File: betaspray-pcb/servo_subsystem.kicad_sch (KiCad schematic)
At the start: 8 parts, among them J11 Conn_01x03_Pin, J12 Conn_01x03_Pin, J13 Conn_01x03_Pin, J14 Conn_01x03_Pin, J15 Conn_01x03_Pin, J16 Conn_01x03_Pin, J17 Conn_01x03_Pin, J18 Conn_01x03_Pin

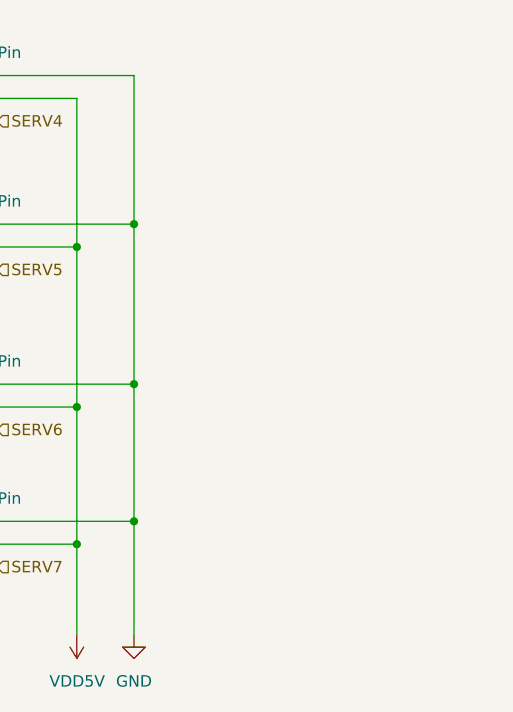
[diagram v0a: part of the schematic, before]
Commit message: Added lasers to schematic and footprint
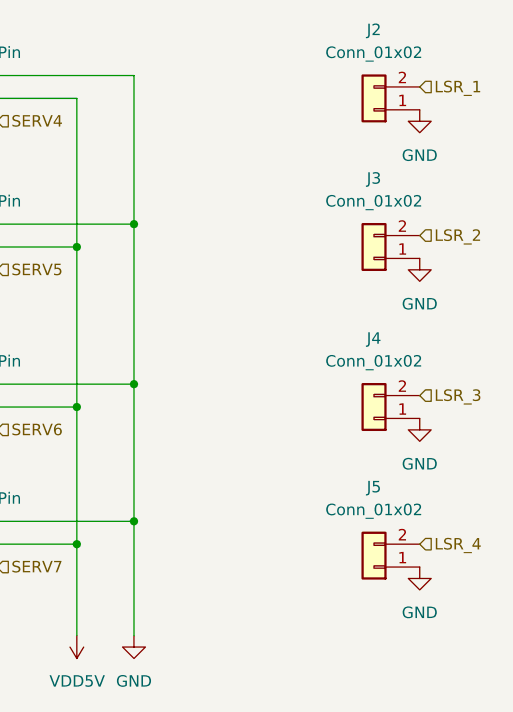
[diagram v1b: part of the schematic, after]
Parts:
- added J2, J3, J4, J5: Conn_01x02, Connector_PinHeader_2.54mm:PinHeader_2x01_P2.54mm_Vertical, symbol betaspray_MCU_Espressif:Conn_01x02
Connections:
- net GND: now also J2.1 (Pin_1), J3.1 (Pin_1), J4.1 (Pin_1), J5.1 (Pin_1)
- new net LSR_1: J2.2 (Pin_2)
- new net LSR_2: J3.2 (Pin_2)
- new net LSR_3: J4.2 (Pin_2)
- new net LSR_4: J5.2 (Pin_2)

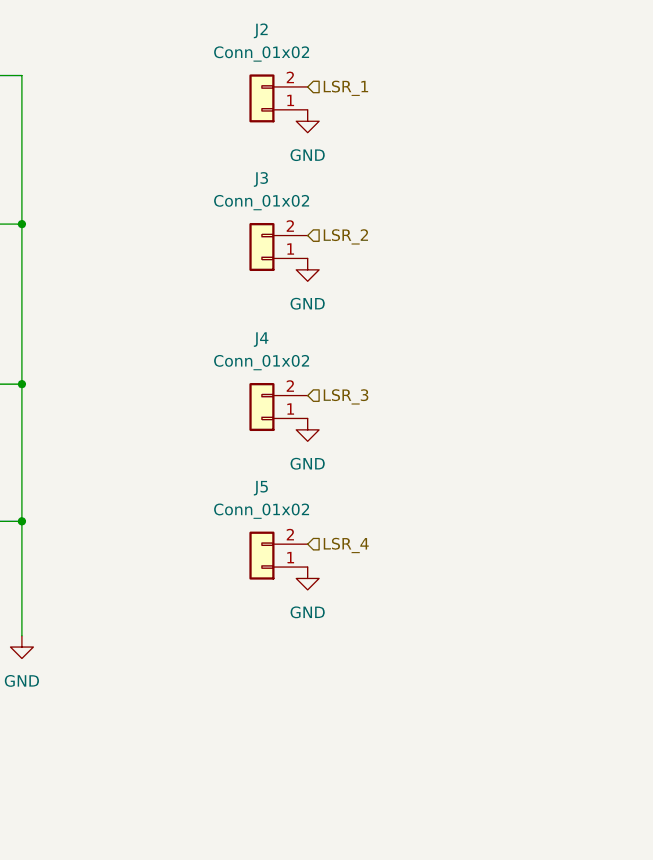
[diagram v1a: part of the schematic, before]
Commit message: Change Laser diode layout
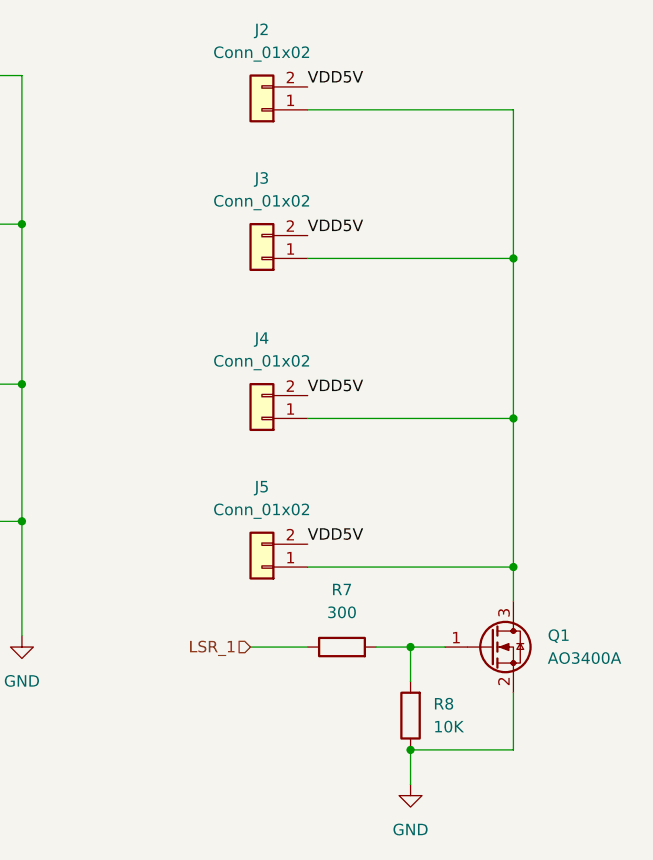
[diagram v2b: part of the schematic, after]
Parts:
- added Q1: AO3400A, Package_TO_SOT_SMD:SOT-23, symbol betaspray_Transistor_FET:AO3400A
- added R7: 300, symbol betaspray_MCU_Espressif:R
- added R8: 10K, symbol betaspray_MCU_Espressif:R
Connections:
- net LSR_2 is gone; now on net VDD5V: J3.2 (Pin_2)
- net LSR_3 is gone; now on net VDD5V: J4.2 (Pin_2)
- net LSR_4 is gone; now on net VDD5V: J5.2 (Pin_2)
- net GND: now also Q1.2 (S), R8.1; no longer J2.1 (Pin_1), J3.1 (Pin_1), J4.1 (Pin_1), J5.1 (Pin_1)
- net LSR_1: now also R7.1; no longer J2.2 (Pin_2)
- net VDD5V: now also J2.2 (Pin_2)
- new net: Q1.1 (G), R7.2, R8.2
- new net: J2.1 (Pin_1), J3.1 (Pin_1), J4.1 (Pin_1), J5.1 (Pin_1), Q1.3 (D)

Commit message: added bulk CAP servos
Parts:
- added C10, C11: 2200uF, symbol betaspray_MCU_Espressif:C
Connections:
- net GND: now also C10.2, C11.2
- net VDD5V: now also C10.1, C11.1

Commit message: Ver0, pls'
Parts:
- C10, C11: footprint (none) -> Capacitor_THT:CP_Radial_D16.0mm_P7.50mm
- R7, R8: footprint (none) -> Resistor_SMD:R_0805_2012Metric_Pad1.20x1.40mm_HandSolder
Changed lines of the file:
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@@
 			)
 		)
-		(property "Footprint" ""
+		(property "Footprint" "Resistor_SMD:R_0805_2012Metric_Pad1.20x1.40mm_HandSolder"
 			(at 154.178 113.03 90)
 			(effects
@@
 			)
 		)
-		(property "Footprint" ""
+		(property "Footprint" "Capacitor_THT:CP_Radial_D16.0mm_P7.50mm"
 			(at 56.8452 129.54 0)
 			(effects
@@
 			)
 		)
-		(property "Footprint" ""
+		(property "Footprint" "Capacitor_THT:CP_Radial_D16.0mm_P7.50mm"
 			(at 35.2552 129.54 0)
 			(effects
@@
 			)
 		)
-		(property "Footprint" ""
+		(property "Footprint" "Resistor_SMD:R_0805_2012Metric_Pad1.20x1.40mm_HandSolder"
 			(at 144.78 107.188 90)
 			(effects

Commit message: Tweak pcb slightly
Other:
- note added: "Laser Drive Circuit"
- note added: "Servo Decoupling Capacitors"
- note added: "Servo PWM Connections"
- moved on the sheet: C10, C11, J11, J12, J13, J14, J15, J16, J17, J18, J2, J3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
